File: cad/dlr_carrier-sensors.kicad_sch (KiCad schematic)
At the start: 15 parts, among them J10 YL-83, J8 FLIR_LEPTON_FFC, J9 SI1145, U5 DHT22, U6 ADS1115

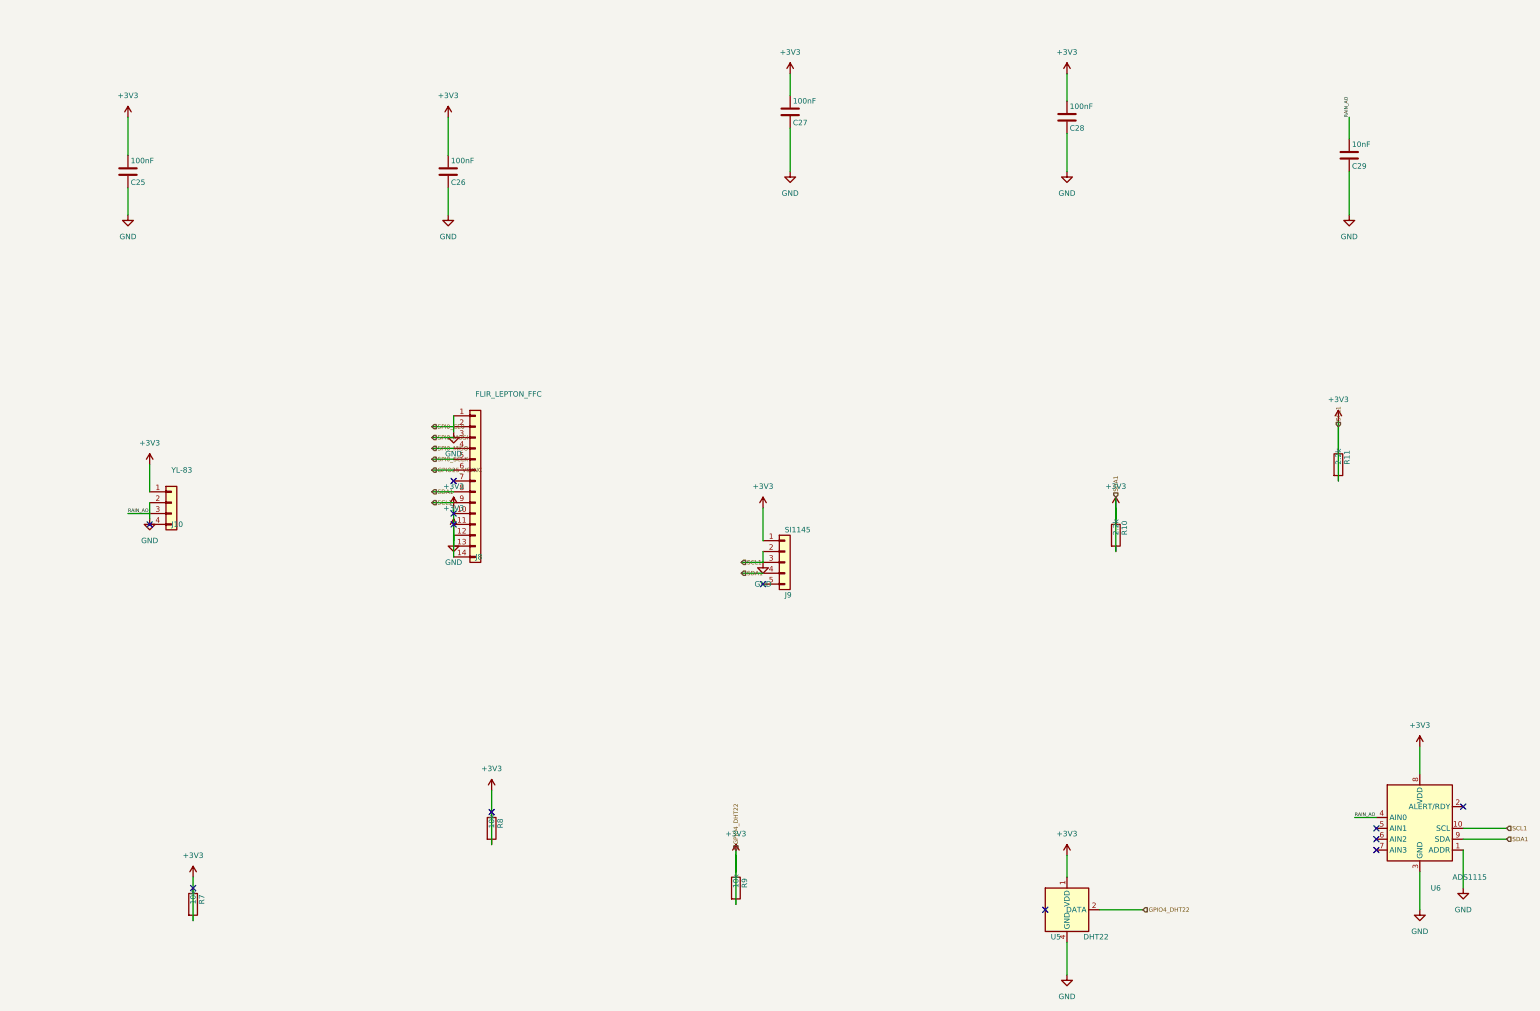
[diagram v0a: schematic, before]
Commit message: 🗺 feat(cad): scripted schematic + board pipeline, 4-layer stack
The committed board had almost every pad on +3V3 — no 5V_RAIL, VBAT or SDA1 net
existed on it at all — so the gerbers in output/ were never a valid board. Cause:
"Update PCB from Schematic" is GUI-only, so nothing kept the board honest, and the
schematic generator itself was merging nets.

Schematic generator:
  * power stubs now run along the pin direction; they used to be forced up or down
    regardless, which drove a 5V_RAIL stub straight through the buck inductor's
    BUCK_SW pin
  * PWR_FLAGs are placed by rule — any net that reaches a power-input pin with no
    power-output pin gets exactly one — instead of a hardcoded list, which is what
    the new VBAT and CHG_VCC rails needed
  * placement is deterministic; it used Python's salted hash(), so no two runs
    produced the same schematic
  * sch_guard fails the build on any cross-net wire/pin collision
  * ~700 lines of dead single-sheet generator removed
  ERC: 0 violations across all 8 sheets.

Board pipeline (cad/drawing/, all scripted, no GUI step):
  sync_pcb      rebuilds every footprint from the library and reassigns every pad
                net from the SKiDL netlist — the replacement for F8
  board_setup   4-layer SIG/GND/5V/SIG stack, rules, net classes, planes (ADR-016)
  route_pcb     DSN -> Freerouting -> SES, after patching the DSN so plane layers
                are "power" (the router was slicing the planes with signals) and
                the plane declarations are dropped (the router had been leaving
                GND and 5V pads with no path to the plane at all)
  stitch_planes vias from surface pads into their plane
  close_gaps    closes what the router leaves, using real segment-to-segment
                clearance; it never forces copper through another net

DRC: 265 unconnected -> 5, with no clearance, short, annular-ring or courtyard
errors. The remaining 5 are escapes on the DF40, the VQFN and the MSOP; they are
l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
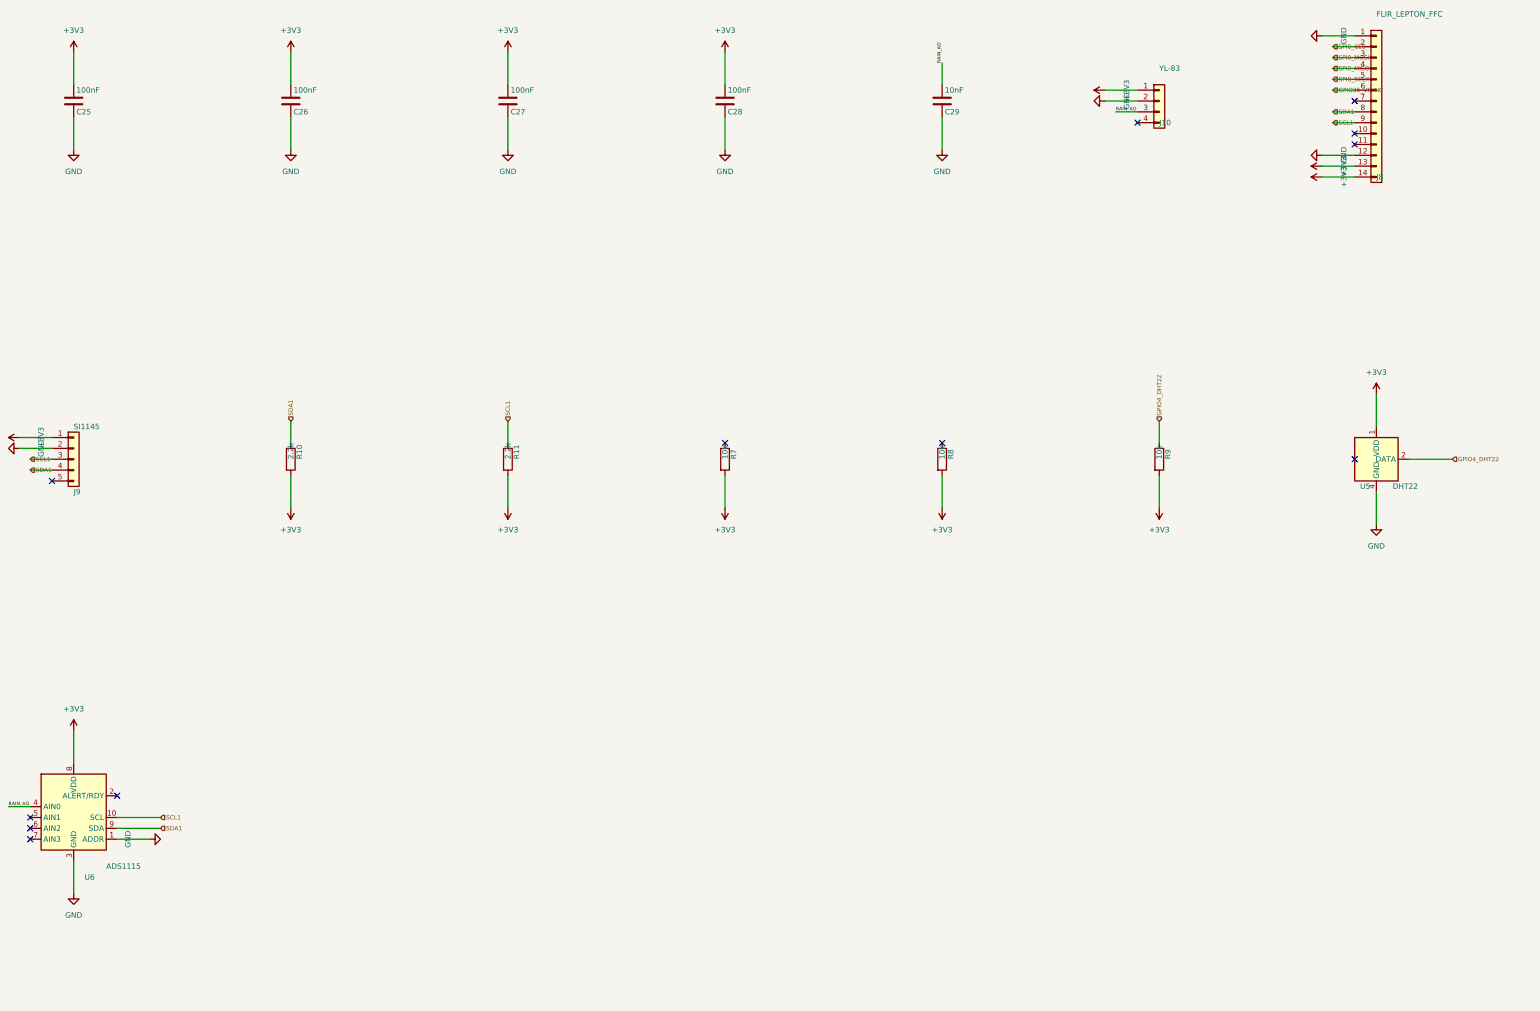
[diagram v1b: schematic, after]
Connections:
- net +3V3: no longer C25.2, C26.2, C27.2, C28.2, C29.2, J10.2 (Pin_2), J8.1 (Pin_1), J8.12 (Pin_12), J8.8 (Pin_8), J8.9 (Pin_9), J9.2 (Pin_2), J9.3 (Pin_3), J9.4 (Pin_4), R10.1, R11.1, R9.1, U5.2 (DATA), U5.4 (GND), U6.1 (ADDR), U6.10 (SCL), U6.3 (GND), U6.9 (SDA)
- new net GND: C25.2, C26.2, C27.2, C28.2, C29.2, J10.2 (Pin_2), J8.1 (Pin_1), J8.12 (Pin_12), J9.2 (Pin_2), U5.4 (GND), U6.1 (ADDR), U6.3 (GND)
- new net GPIO4_DHT22: R9.1, U5.2 (DATA)
- new net SCL1: J8.9 (Pin_9), J9.3 (Pin_3), R11.1, U6.10 (SCL)
- new net SDA1: J8.8 (Pin_8), J9.4 (Pin_4), R10.1, U6.9 (SDA)
